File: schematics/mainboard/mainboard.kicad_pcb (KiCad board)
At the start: 2 copper layers, 86.1 x 79.8 mm, 36 parts, among them J1 ICSP, J2 USB_B_Micro, J3 DEALON DC-S050-200, J4 PWR_SELECT, J5 JOY1, J6 JOY2, J7 Conn_01x06_Pin, J8 DGAUGES, J9 LCD, U1 ATmega2560-16A, U2 FT232RL, U3 USBLC6-2P6, U4 AIP78M05, U5 L9110, Y1 16Mhz

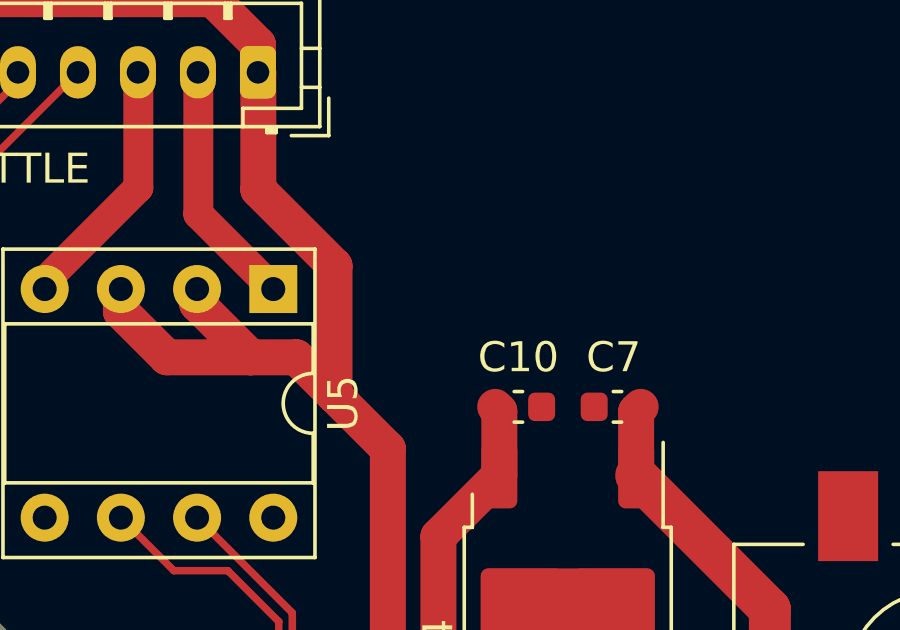
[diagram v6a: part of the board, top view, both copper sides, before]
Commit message: SCH: Mainboard: add power LED
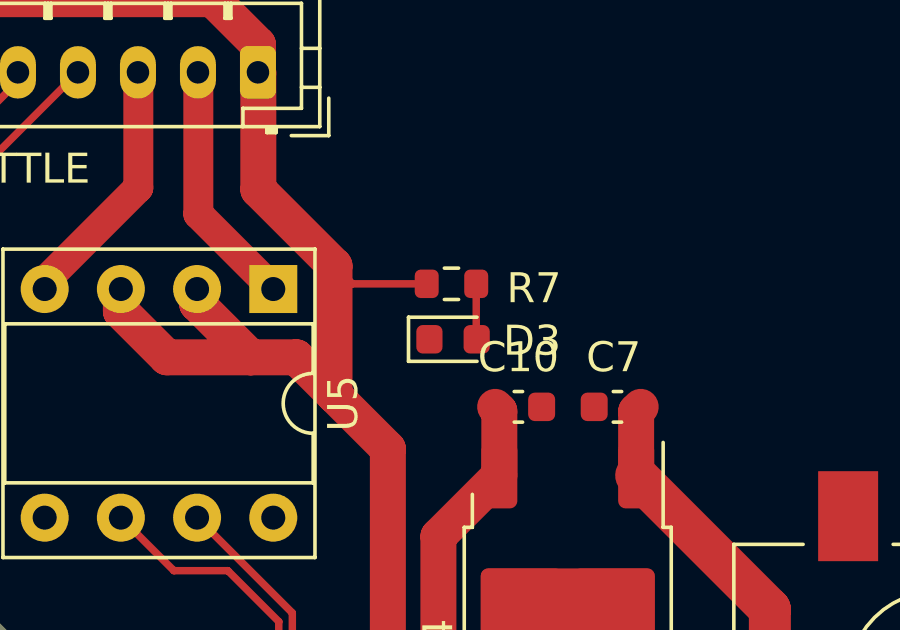
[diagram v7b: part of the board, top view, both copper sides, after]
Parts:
- added D3: GREEN ON, LED_SMD:LED_0603_1608Metric, F.Cu at (178.7, 37.5)
- added R7: 1k, Resistor_SMD:R_0603_1608Metric, F.Cu at (178.7, 35.6)
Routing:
- net +5V: track 270.7 -> 274.1 mm
- net Net-(D3-A): track 0.00 -> 1.86 mm
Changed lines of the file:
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@@
   (net 122 "Net-(U1-PG0)")
   (net 123 "Net-(U2-3V3OUT)")
+  (net 124 "Net-(D3-A)")
   (footprint "Package_TO_SOT_SMD:TO-252-2" (layer "F.Cu")
     (at 182.526 47.077 -90)
@@
     )
   )
+  (footprint "LED_SMD:LED_0603_1608Metric" (layer "F.Cu")
+    (at 178.7025 37.49875)
+    (descr "LED SMD 0603 (1608 Metric), square (rectangular) end terminal, IPC_7351 nominal, (Body size source: http://www.tortai-tech.com/upload/download/2011102023233369053.pdf), generated with kicad-footprint-generator")
+    (tags "LED")
+    (property "Sheetfile" "mainboard.kicad_sch")
+    (property "Sheetname" "")
+    (property "ki_description" "Light emitting diode")
+    (property "ki_keywords" "LED diode")
+    (attr smd)
+    (fp_text reference "D3" (at 2.635 0.05) (layer "F.SilkS")
+        (effects (font (size 1 1) (thickness 0.15)))
+    )
+    (fp_text value "GREEN ON" (at -1.14 -1.575) (layer "F.Fab")
+        (effects (font (size 1 1) (thickness 0.15)))
+    )
+    (fp_text user "${REFERENCE}" (at 0 0) (layer "F.Fab")
+        (effects (font (size 0.4 0.4) (thickness 0.06)))
+    )
+    (fp_line (start -1.485 -0.735) (end -1.485 0.735)
+      (stroke (width 0.12) (type solid)) (layer "F.SilkS"))
+    (fp_line (start -1.485 0.735) (end 0.8 0.735)
+      (stroke (width 0.12) (type solid)) (layer "F.SilkS"))
+    (fp_line (start 0.8 -0.735) (end -1.485 -0.735)
+      (stroke (width 0.12) (type solid)) (layer "F.SilkS"))
+    (fp_line (start -1.48 -0.73) (end 1.48 -0.73)
+      (stroke (width 0.05) (type solid)) (layer "F.CrtYd"))
+    (fp_line (start -1.48 0.73) (end -1.48 -0.73)
+      (stroke (width 0.05) (type solid)) (layer "F.CrtYd"))
+    (fp_line (start 1.48 -0.73) (end 1.48 0.73)
+      (stroke (width 0.05) (type solid)) (layer "F.CrtYd"))
+    (fp_line (start 1.48 0.73) (end -1.48 0.73)
+      (stroke (width 0.05) (type solid)) (layer "F.CrtYd"))
+    (fp_line (start -0.8 -0.1) (end -0.8 0.4)
+      (stroke (width 0.1) (type solid)) (layer "F.Fab"))
+    (fp_line (start -0.8 0.4) (end 0.8 0.4)
+      (stroke (width 0.1) (type solid)) (layer "F.Fab"))
+    (fp_line (start -0.5 -0.4) (end -0.8 -0.1)
+      (stroke (width 0.1) (type solid)) (layer "F.Fab"))
+    (fp_line (start 0.8 -0.4) (end -0.5 -0.4)
+      (stroke (width 0.1) (type solid)) (layer "F.Fab"))
+    (fp_line (start 0.8 0.4) (end 0.8 -0.4)
+      (stroke (width 0.1) (type solid)) (layer "F.Fab"))
+    (pad "1" smd roundrect (at -0.7875 0) (size 0.875 0.95) (layers "F.Cu" "F.Paste" "F.Mask") (roundrect_rratio 0.25)
+      (net 93 "GND") (pinfunction "K") (pintype "passive"))
+    (pad "2" smd roundrect (at 0.7875 0) (size 0.875 0.95) (layers "F.Cu" "F.Paste" "F.Mask") (roundrect_rratio 0.25)
+      (net 124 "Net-(D3-A)") (pinfunction "A") (pintype "passive"))
+    (model "${KICAD6_3DMODEL_DIR}/LED_SMD.3dshapes/LED_0603_1608Metric.wrl"
+      (offset (xyz 0 0 0))
+      (scale (xyz 1 1 1))
+      (rotate (xyz 0 0 0))
+    )
+  )
   (footprint "Resistor_SMD:R_0603_1608Metric" (layer "F.Cu")
     (at 186.596 73.723 -90)
@@
     )
   )
+  (footprint "Resistor_SMD:R_0603_1608Metric" (layer "F.Cu")
+    (at 178.65 35.65 180)
+    (descr "Resistor SMD 0603 (1608 Metric), square (rectangular) end terminal, IPC_7351 nominal, (Body size source: IPC-SM-782 page 72, https://www.pcb-3d.com/wordpress/wp-content/uploads/ipc-sm-782a_amendment_1_and_2.pdf), generated with kicad-footprint-generator")
+    (tags "resistor")
+    (property "Sheetfile" "mainboard.kicad_sch")
+    (property "Sheetname" "")
+    (property "ki_description" "Resistor")
+    (property "ki_keywords" "R res resistor")
+    (property "lcsc" "C21190")
+    (attr smd)
+    (fp_text reference "R7" (at -2.75 -0.15) (layer "F.SilkS")
+        (effects (font (size 1 1) (thickness 0.15)))
+    )
+    (fp_text value "1k" (at 0 1.43) (layer "F.Fab") hide
+        (effects (font (size 1 1) (thickness 0.15)))
+    )
+    (fp_text user "${REFERENCE}" (at 0 0) (layer "F.Fab")
+        (effects (font (size 0.4 0.4) (thickness 0.06)))
+    )
+    (fp_line (start -0.237258 -0.5225) (end 0.237258 -0.5225)
+      (stroke (width 0.12) (type solid)) (layer "F.SilkS"))
+    (fp_line (start -0.237258 0.5225) (end 0.237258 0.5225)
+      (stroke (width 0.12) (type solid)) (layer "F.SilkS"))
+    (fp_line (start -1.48 -0.73) (end 1.48 -0.73)
+      (stroke (width 0.05) (type solid)) (layer "F.CrtYd"))
+    (fp_line (start -1.48 0.73) (end -1.48 -0.73)
+      (stroke (width 0.05) (type solid)) (layer "F.CrtYd"))
+    (fp_line (start 1.48 -0.73) (end 1.48 0.73)
+      (stroke (width 0.05) (type solid)) (layer "F.CrtYd"))
+    (fp_line (start 1.48 0.73) (end -1.48 0.73)
+      (stroke (width 0.05) (type solid)) (layer "F.CrtYd"))
+    (fp_line (start -0.8 -0.4125) (end 0.8 -0.4125)
+      (stroke (width 0.1) (type solid)) (layer "F.Fab"))
+    (fp_line (start -0.8 0.4125) (end -0.8 -0.4125)
+      (stroke (width 0.1) (type solid)) (layer "F.Fab"))
+    (fp_line (start 0.8 -0.4125) (end 0.8 0.4125)
+      (stroke (width 0.1) (type solid)) (layer "F.Fab"))
+    (fp_line (start 0.8 0.4125) (end -0.8 0.4125)
+      (stroke (width 0.1) (type solid)) (layer "F.Fab"))
+    (pad "1" smd roundrect (at -0.825 0 180) (size 0.8 0.95) (layers "F.Cu" "F.Paste" "F.Mask") (roundrect_rratio 0.25)
+      (net 124 "Net-(D3-A)") (pintype "passive"))
+    (pad "2" smd roundrect (at 0.825 0 180) (size 0.8 0.95) (layers "F.Cu" "F.Paste" "F.Mask") (roundrect_rratio 0.25)
+      (net 89 "+5V") (pintype "passive"))
+    (model "${KICAD6_3DMODEL_DIR}/Resistor_SMD.3dshapes/R_0603_1608Metric.wrl"
+      (offset (xyz 0 0 0))
+      (scale (xyz 1 1 1))
+      (rotate (xyz 0 0 0))
+    )
+  )
   (footprint "Connector_USB:USB_Micro-B_Molex-105017-0001" (layer "F.Cu")
     (at 201.7847 67.594 90)
@@
   (segment (start 162.156 67.874) (end 158.91 71.12) (width 0.25) (layer "F.Cu") (net 89))
   (segment (start 174.752 39.37) (end 173.482 38.1) (width 1.2) (layer "F.Cu") (net 89))
+  (segment (start 175.35 35.65) (end 174.752 35.052) (width 0.25) (layer "F.Cu") (net 89))
+  (segment (start 174.77575 35.02825) (end 174.752 35.052) (width 0.4) (layer "F.Cu") (net 89))
   (segment (start 158.91 71.12) (end 158.91 71.026) (width 0.25) (layer "F.Cu") (net 89))
   (segment (start 162.156 59.365) (end 162.466 59.055) (width 0.25) (layer "F.Cu") (net 89))
@@
   (segment (start 185.59 72.29) (end 185.59 73.57) (width 0.35) (layer "F.Cu") (net 89))
   (segment (start 144.018 28.702) (end 144.018 27.686) (width 1.2) (layer "F.Cu") (net 89))
+  (segment (start 177.825 35.65) (end 175.35 35.65) (width 0.25) (layer "F.Cu") (net 89))
   (segment (start 158.91 71.026) (end 156.718 68.834) (width 0.25) (layer "F.Cu") (net 89))
   (segment (start 170.17 36.312) (end 170.17 35.824) (width 1.2) (layer "F.Cu") (net 89))
@@
   (segment (start 190.3 69.83704) (end 190.3 70.95) (width 0.25) (layer "B.Cu") (net 123))
   (segment (start 189.406084 66.282) (end 189.406084 67.403977) (width 0.25) (layer "B.Cu") (net 123))
+  (segment (start 179.4775 35.6475) (end 179.475 35.65) (width 0.25) (layer "F.Cu") (net 124))
+  (segment (start 179.475 37.48375) (end 179.49 37.49875) (width 0.25) (layer "F.Cu") (net 124))
+  (segment (start 179.475 35.65) (end 179.475 37.48375) (width 0.25) (layer "F.Cu") (net 124))
   (zone (net 93) (net_name "GND") (layer "F.Cu") (hatch edge 0.5)
     (connect_pads (clearance 0.2))

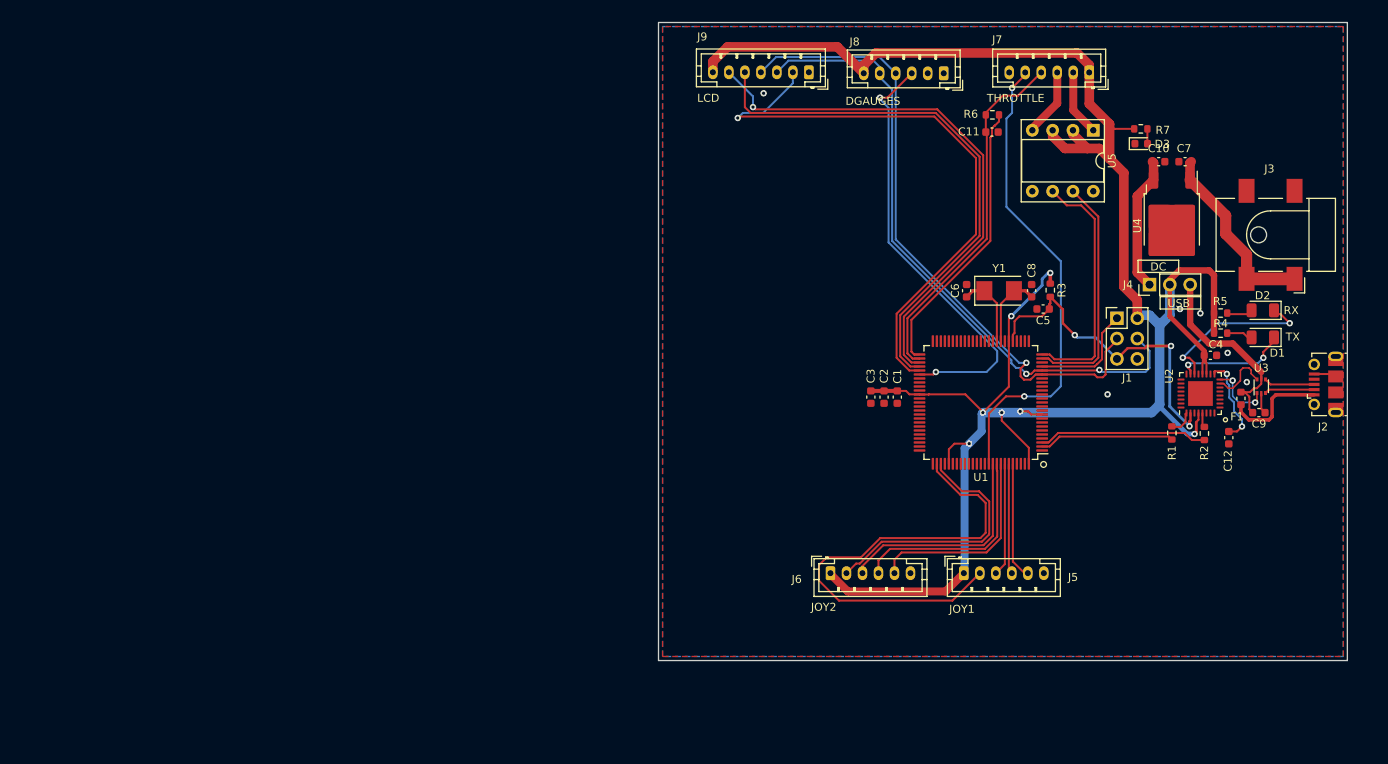
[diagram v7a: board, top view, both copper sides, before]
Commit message: SCH: Mainboard=> LED routing (1)
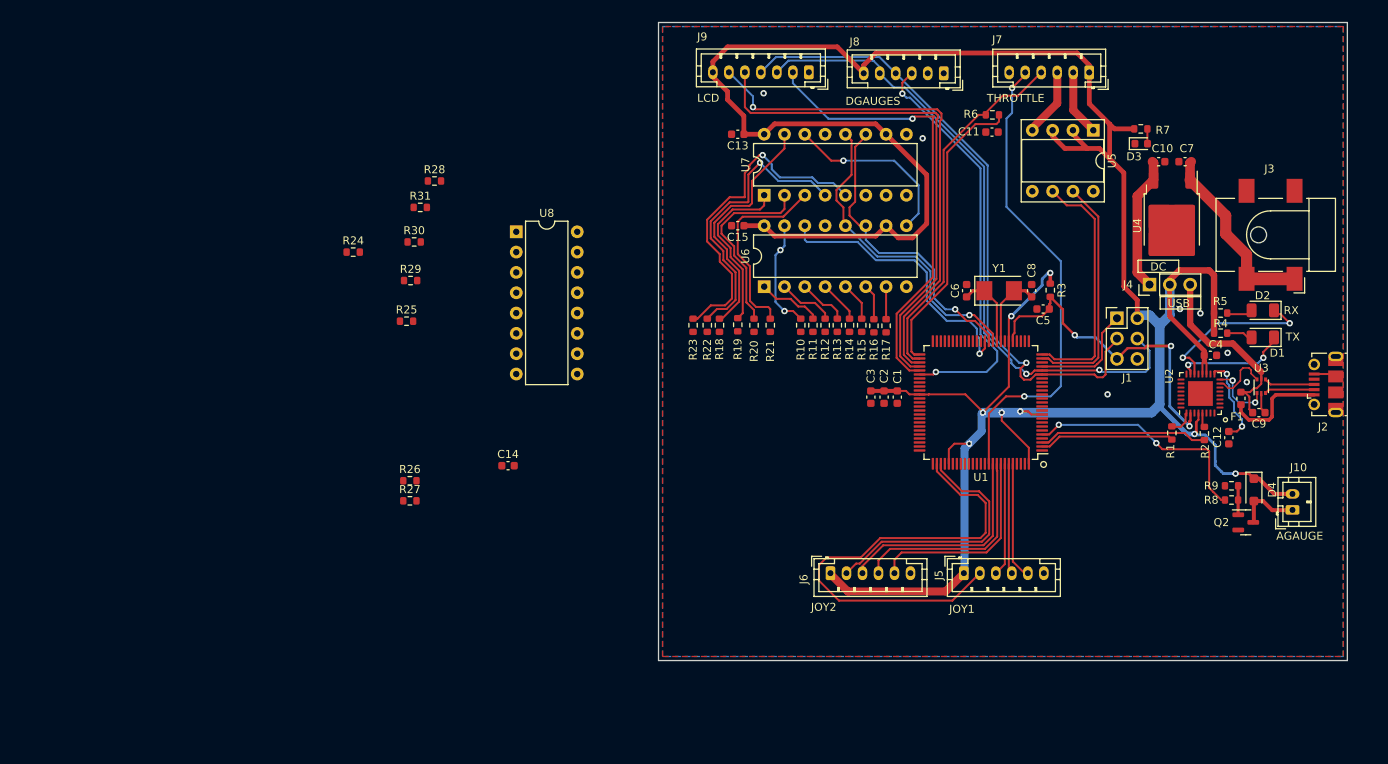
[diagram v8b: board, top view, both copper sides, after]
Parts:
- added C13: 0.1 µf, Capacitor_SMD:C_0603_1608Metric, F.Cu at (128.3, 36.3)
- added C14: 0.1 µf, Capacitor_SMD:C_0603_1608Metric, F.Cu at (99.6, 77.8)
- added C15: 0.1 µf, Capacitor_SMD:C_0603_1608Metric, F.Cu at (128.3, 47.8)
- added D4: 1N4002, Diode_SMD:D_SOD-123F, F.Cu at (192.8, 80.8)
- added J10: Conn_01x02_Pin, Connector_JST:JST_PH_B2B-PH-K_1x02_P2.00mm_Vertical, F.Cu at (197.6, 83.3)
- added Q2: BC849, Package_TO_SOT_SMD:SOT-23, F.Cu at (191.8, 84.8)
- added R10: R?, Resistor_SMD:R_0603_1608Metric, F.Cu at (136.1, 60.2)
- added R11: R?, Resistor_SMD:R_0603_1608Metric, F.Cu at (137.7, 60.2)
- added R12: R?, Resistor_SMD:R_0603_1608Metric, F.Cu at (139.2, 60.2)
- added R13: R?, Resistor_SMD:R_0603_1608Metric, F.Cu at (140.7, 60.2)
- added R14: R?, Resistor_SMD:R_0603_1608Metric, F.Cu at (142.2, 60.2)
- added R15: R?, Resistor_SMD:R_0603_1608Metric, F.Cu at (143.8, 60.2)
- added R16: R?, Resistor_SMD:R_0603_1608Metric, F.Cu at (145.3, 60.3)
- added R17: R?, Resistor_SMD:R_0603_1608Metric, F.Cu at (146.8, 60.3)
- added R18: R?, Resistor_SMD:R_0603_1608Metric, F.Cu at (126.0, 60.2)
- added R19: R?, Resistor_SMD:R_0603_1608Metric, F.Cu at (128.3, 60.1)
- added R20: R?, Resistor_SMD:R_0603_1608Metric, F.Cu at (130.3, 60.2)
- added R21: R?, Resistor_SMD:R_0603_1608Metric, F.Cu at (132.3, 60.2)
- added R22: R?, Resistor_SMD:R_0603_1608Metric, F.Cu at (124.5, 60.2)
- added R23: R?, Resistor_SMD:R_0603_1608Metric, F.Cu at (122.7, 60.2)
- added R24: R?, Resistor_SMD:R_0603_1608Metric, F.Cu at (80.2, 51.1)
- added R25: R?, Resistor_SMD:R_0603_1608Metric, F.Cu at (86.9, 59.7)
- added R26: R?, Resistor_SMD:R_0603_1608Metric, F.Cu at (87.3, 79.6)
- added R27: R?, Resistor_SMD:R_0603_1608Metric, F.Cu at (87.3, 82.1)
- added R28: R?, Resistor_SMD:R_0603_1608Metric, F.Cu at (90.4, 42.2)
- added R29: R?, Resistor_SMD:R_0603_1608Metric, F.Cu at (87.4, 54.6)
- added R30: R?, Resistor_SMD:R_0603_1608Metric, F.Cu at (87.8, 49.8)
- added R31: R?, Resistor_SMD:R_0603_1608Metric, F.Cu at (88.6, 45.5)
- added R8: 470, Resistor_SMD:R_0603_1608Metric, F.Cu at (190.0, 82.0)
- added R9: 10K, Resistor_SMD:R_0603_1608Metric, F.Cu at (190.0, 80.3)
- added U6: 74HC595, Package_DIP:DIP-16_W7.62mm, F.Cu at (131.6, 55.4)
- added U7: 74HC595, Package_DIP:DIP-16_W7.62mm, F.Cu at (131.6, 43.9)
- added U8: 74HC165, Package_DIP:DIP-16_W7.62mm, F.Cu at (100.6, 48.5)
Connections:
- U1 pad 35: unconnected-(U1-PL0-Pad35) -> Net-(U1-PL0)
- U1 pad 36: unconnected-(U1-PL1-Pad36) -> Net-(U1-PL1)
- U1 pad 37: unconnected-(U1-PL2-Pad37) -> Net-(U1-PL2)
- U1 pad 5: unconnected-(U1-PE3-Pad5) -> Net-(U1-PE3)
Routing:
- net +5V: track 274.1 -> 357.7 mm, vias 7 -> 8
- net Net-(U7-QF): track 0.00 -> 42.1 mm, vias 0 -> 1
- net Net-(U1-PL0): track 0.00 -> 40.0 mm, vias 0 -> 1
- net Net-(U1-PL1): track 0.00 -> 38.5 mm, vias 0 -> 1
- net Net-(U7-QE): track 0.00 -> 36.7 mm, vias 0 -> 1
- net Net-(U1-PL2): track 0.00 -> 35.1 mm, vias 0 -> 1
- net Net-(U7-QA): track 0.00 -> 30.5 mm
- net Net-(U1-PE3): track 0.00 -> 29.9 mm, vias 0 -> 2
- net Net-(U7-QD): track 0.00 -> 24.5 mm
- net Net-(U7-QC): track 0.00 -> 23.8 mm
- net Net-(U6-QH'): track 0.00 -> 22.6 mm, vias 0 -> 1
- net Net-(U7-QB): track 0.00 -> 21.3 mm
- net Net-(J9-Pin_2): track 74.7 -> 56.6 mm
- net Net-(U6-QA): track 0.00 -> 14.0 mm, vias 0 -> 2
- net Net-(U6-QB): track 0.00 -> 8.05 mm
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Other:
- board text added: "AGAUGE"
